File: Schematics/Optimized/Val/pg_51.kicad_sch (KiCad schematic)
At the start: 35 parts, among them U3501 F175, U3502 F175, U3503 F175, U5301 F158, U5302 F157, U5303 F02, U5304 F02, U5305 F74, U5306 F74, U5307 F02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

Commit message: TYP+VAL condensation
Tested: passed expmon_test_val (-muxbus)
Tested: passed expmon_test_typ (-muxbus)
Tested: passed run_udiag
Tested: passed boot_env (R2_INTEG until PRETTY_PRINTER)
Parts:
- removed U3501, U3502, U3503: F175, symbol r1000:F175
- removed U5301, U5401: F158, symbol r1000:F158
- removed U5302, U5310, U5311, U5312, U5406, U5408, U5410, U5411: F157, symbol r1000:F157
- removed U5303, U5304: F02, symbol r1000:F02
- removed U5313: F381, symbol r1000:F381
- removed U5407, U5421, U5422: F283, symbol r1000:F283
- removed U5409: F00, symbol r1000:F00
- removed U5420: F181, symbol r1000:F181
- added U2602: XCADR, symbol r1000:XCADR
- added U2609, U2616: F521, symbol r1000:F521
- added U2610, U2617: F74, symbol r1000:F74
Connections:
- net C.ALU.SEL0: now also U2602.74 (CTL0)
- net C.ALU.SEL1: now also U2602.75 (CTL1)
- net C.ALU.SEL2: now also U2602.76 (CTL2)
- net C.CSA.SEL: now also U2602.77 (CTL3)
- net C.LOOP.SEL: now also U2602.78 (CTL4)
- net C.ZERO.SEL: now also U2602.79 (CTL5)
- net CSA.DIAG0: now also U2602.21 (CSDG0)
- net CSA.DIAG1: now also U2602.23 (CSDG1)
- net CSA.DIAG2: now also U2602.25 (CSDG2)
- net CSA~.SCLK: now also U2602.4 (CCLK)
- net DIAG.D0: now also U2602.13 (DIAG0)
- net DIAG.D1: now also U2602.15 (DIAG1)
- net DIAG.D2: now also U2602.17 (DIAG2)
- net DIAG.D3: now also U2602.18 (DIAG3)
- net DIAG_MODE: now also U2602.10 (DMODE)
- net LOOP_CNT0: now also U2602.64 (LOOP0)
- net LOOP_CNT1: now also U2602.65 (LOOP1)
- net LOOP_CNT2: now also U2602.66 (LOOP2)
- net LOOP_CNT3: now also U2602.67 (LOOP3)
- net LOOP_CNT4: now also U2602.68 (LOOP4)
- net LOOP_CNT5: now also U2602.69 (LOOP5)
- net LOOP_CNT6: now also U2602.70 (LOOP6)
- net LOOP_CNT7: now also U2602.71 (LOOP7)
- net LOOP_CNT8: now also U2602.72 (LOOP8)
- net LOOP_CNT9: now also U2602.73 (LOOP9)
- net PD: now also U2609.1 (E), U2609.12 (B4), U2609.14 (B5), U2609.7 (B2), U2616.1 (E), U2616.12 (B4), U2616.14 (B5), U2616.7 (B2)
- net UIR.A2: now also U2602.32 (A2)
- net UIR.A3: now also U2602.34 (A3)
- net UIR.A4: now also U2602.36 (A4)
- net UIR.A5: now also U2602.37 (A5)
- net UIR.B2: now also U2602.44 (B2)
- net UIR.B3: now also U2602.46 (B3)
- net UIR.B4: now also U2602.47 (B4)
- net UIR.B5: now also U2602.49 (B5)
- net UIR.C0: now also U2602.51 (C0)
- net UIR.C1: now also U2602.52 (C1)
- net UIR.C2: now also U2602.53 (C2)
- net UIR.C3: now also U2602.54 (C3)
- net UIR.C4: now also U2602.55 (C4)
- net UIR.C5: now also U2602.56 (C5)
- net UIR.FRAME0: now also U2602.38 (FRM0)
- net UIR.FRAME1: now also U2602.39 (FRM1)
- net UIR.FRAME2: now also U2602.41 (FRM2)
- net UIR.FRAME3: now also U2602.43 (FRM3)
- net UIR.FRAME4: now also U2602.45 (FRM4)
- net UIR~.SCLK: now also U2602.1 (UCLK), U2610.3 (CLK), U2617.3 (CLK)
- net V.CSA.OFFS0: now also U2602.60 (CSAO0)
- net V.CSA.OFFS1: now also U2602.61 (CSAO1)
- net V.CSA.OFFS2: now also U2602.62 (CSAO2)
- net V.CSA.OFFS3: now also U2602.63 (CSAO3)
- net V.LOAD_BOT~: now also U2602.57 (LBOT)
- net V.LOAD_TOP~: now also U2602.58 (LTOP)
- net V.POP_DOWN~: now also U2602.59 (LPOP)
- new net: U2616.19 (A=B), U2617.2 (D)
- new net: U2609.19 (A=B), U2610.2 (D)
- new net ARF.ADR0: U2602.2 (AADR0)
- new net ARF.ADR1: U2602.3 (AADR1)
- new net ARF.ADR2: U2602.5 (AADR2)
- new net ARF.ADR3: U2602.6 (AADR3)
- new net ARF.ADR4: U2602.8 (AADR4)
- new net ARF.ADR5: U2602.9 (AADR5)
- new net ARF.ADR6: U2602.11 (AADR6)
- new net ARF.ADR7: U2602.12 (AADR7)
- new net ARF.ADR8: U2602.14 (AADR8)
- new net ARF.ADR9: U2602.16 (AADR9)
- new net A_LOOP_DEC: U2602.48 (ALOOP), U2617.6 (Q_)
- new net BRF.ADR0: U2602.19 (BADR0)
- new net BRF.ADR1: U2602.20 (BADR1)
- new net BRF.ADR2: U2602.22 (BADR2)
- new net BRF.ADR3: U2602.24 (BADR3)
- new net BRF.ADR4: U2602.26 (BADR4)
- new net BRF.ADR5: U2602.27 (BADR5)
- new net BRF.ADR6: U2602.29 (BADR6)
- new net BRF.ADR7: U2602.31 (BADR7)
- new net BRF.ADR8: U2602.33 (BADR8)
- new net BRF.ADR9: U2602.35 (BADR9)
- new net B_LOOP_DEC: U2602.50 (BLOOP), U2610.6 (Q_)
- new net H2: U2602.7 (H2)
- new net UIR.A0: U2602.28 (A0)
- new net UIR.A1: U2602.30 (A1)
- new net UIR.B0: U2602.40 (B0)
- new net UIR.B1: U2602.42 (B1)
- new net WCS.D0: U2616.6 (A2)
- new net WCS.D1: U2616.8 (A3)
- new net WCS.D10: U2609.15 (A6)
- new net WCS.D11: U2609.17 (A7)
- new net WCS.D2: U2616.11 (A4)
- new net WCS.D3: U2616.13 (A5)
- new net WCS.D4: U2616.15 (A6)
- new net WCS.D5: U2616.17 (A7)
- new net WCS.D6: U2609.6 (A2)
- new net WCS.D7: U2609.8 (A3)
- new net WCS.D8: U2609.11 (A4)
- new net WCS.D9: U2609.13 (A5)
- no-connect marks 44 -> 26
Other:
- note added: "UIR.A0"
- note added: "UIR.A1"
- note added: "UIR.A2"
- note added: "UIR.A3"
- note added: "UIR.A4"
- note added: "UIR.A5"
- note added: "UIR.B0"
- note added: "UIR.B1"
- note added: "UIR.B2"
- note added: "UIR.B3"
- note added: "UIR.B4"
- note added: "UIR.B5"
- moved on the sheet: GB11, GB13, GB17, GB3, GB4, GB5, GB6, GB7, GB8, U5305, U5306, U5307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

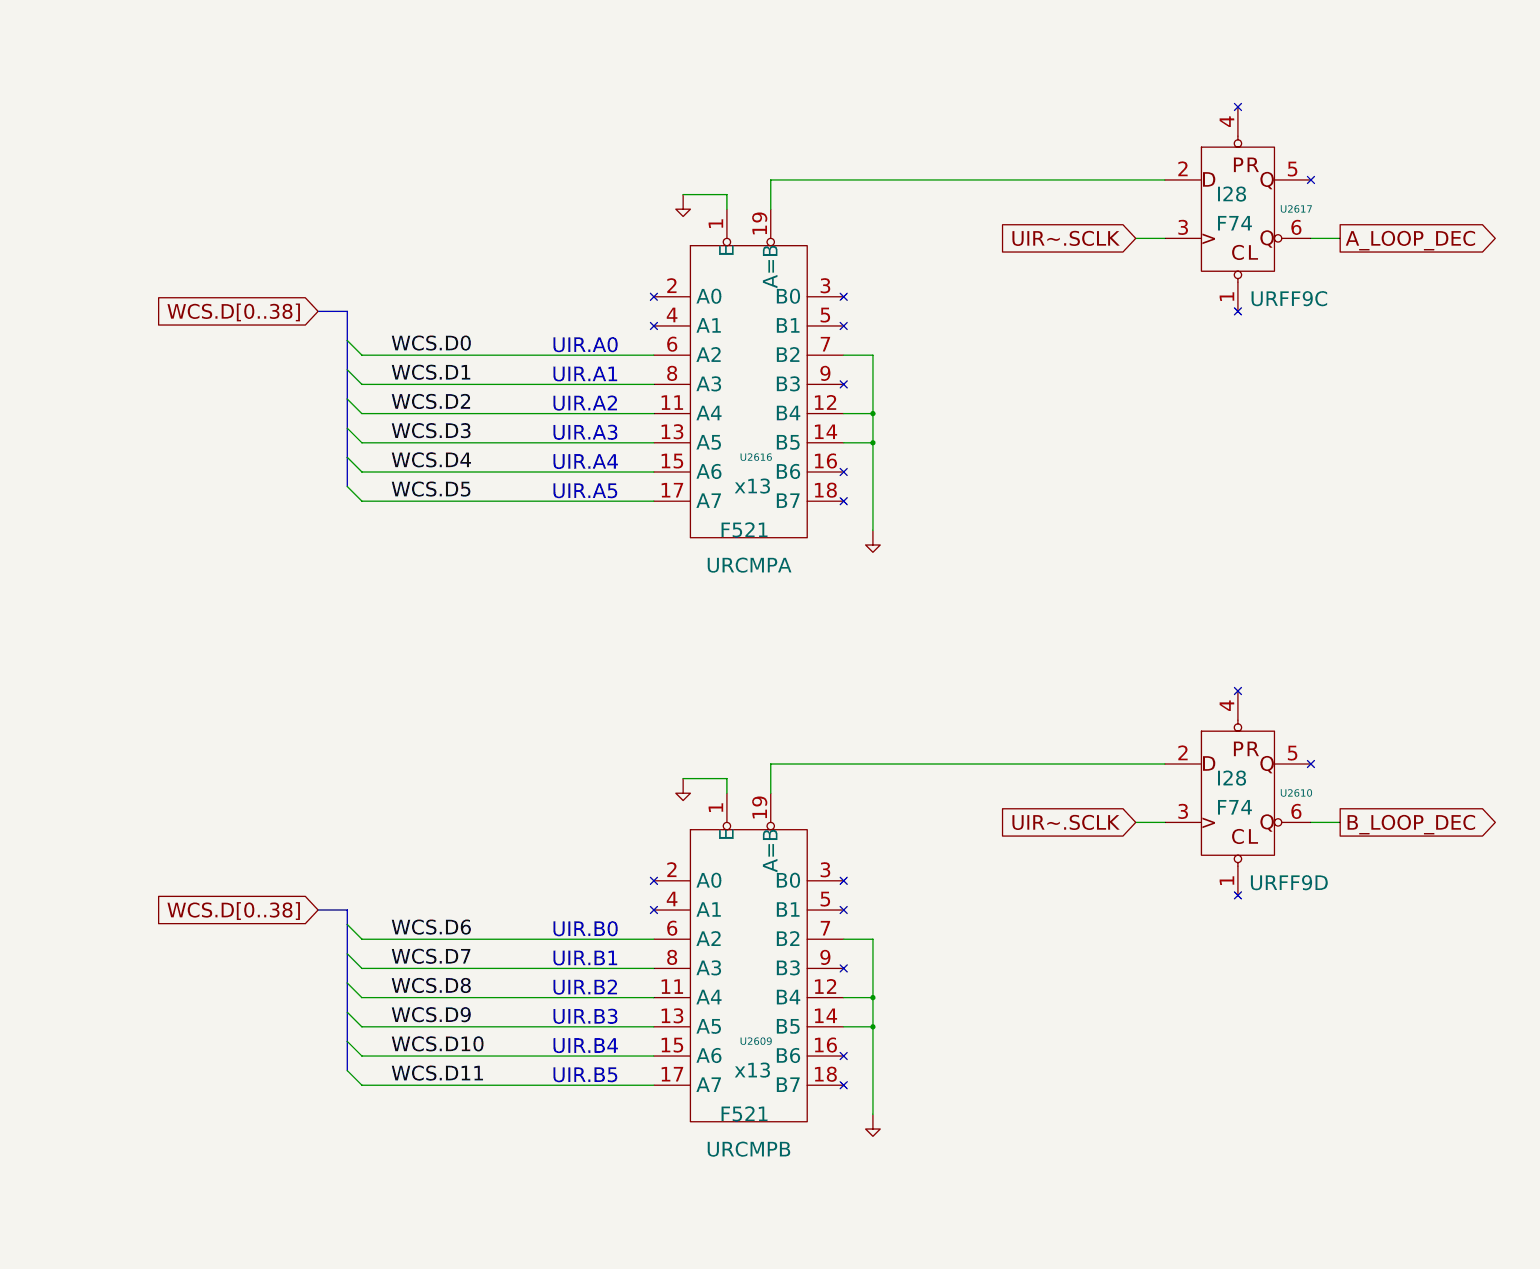
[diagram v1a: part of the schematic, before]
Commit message: Optimization of TYP & VAL
Tested: boot_env (until PRETTY_PRINTER assert)
Tested: passed run_udiag
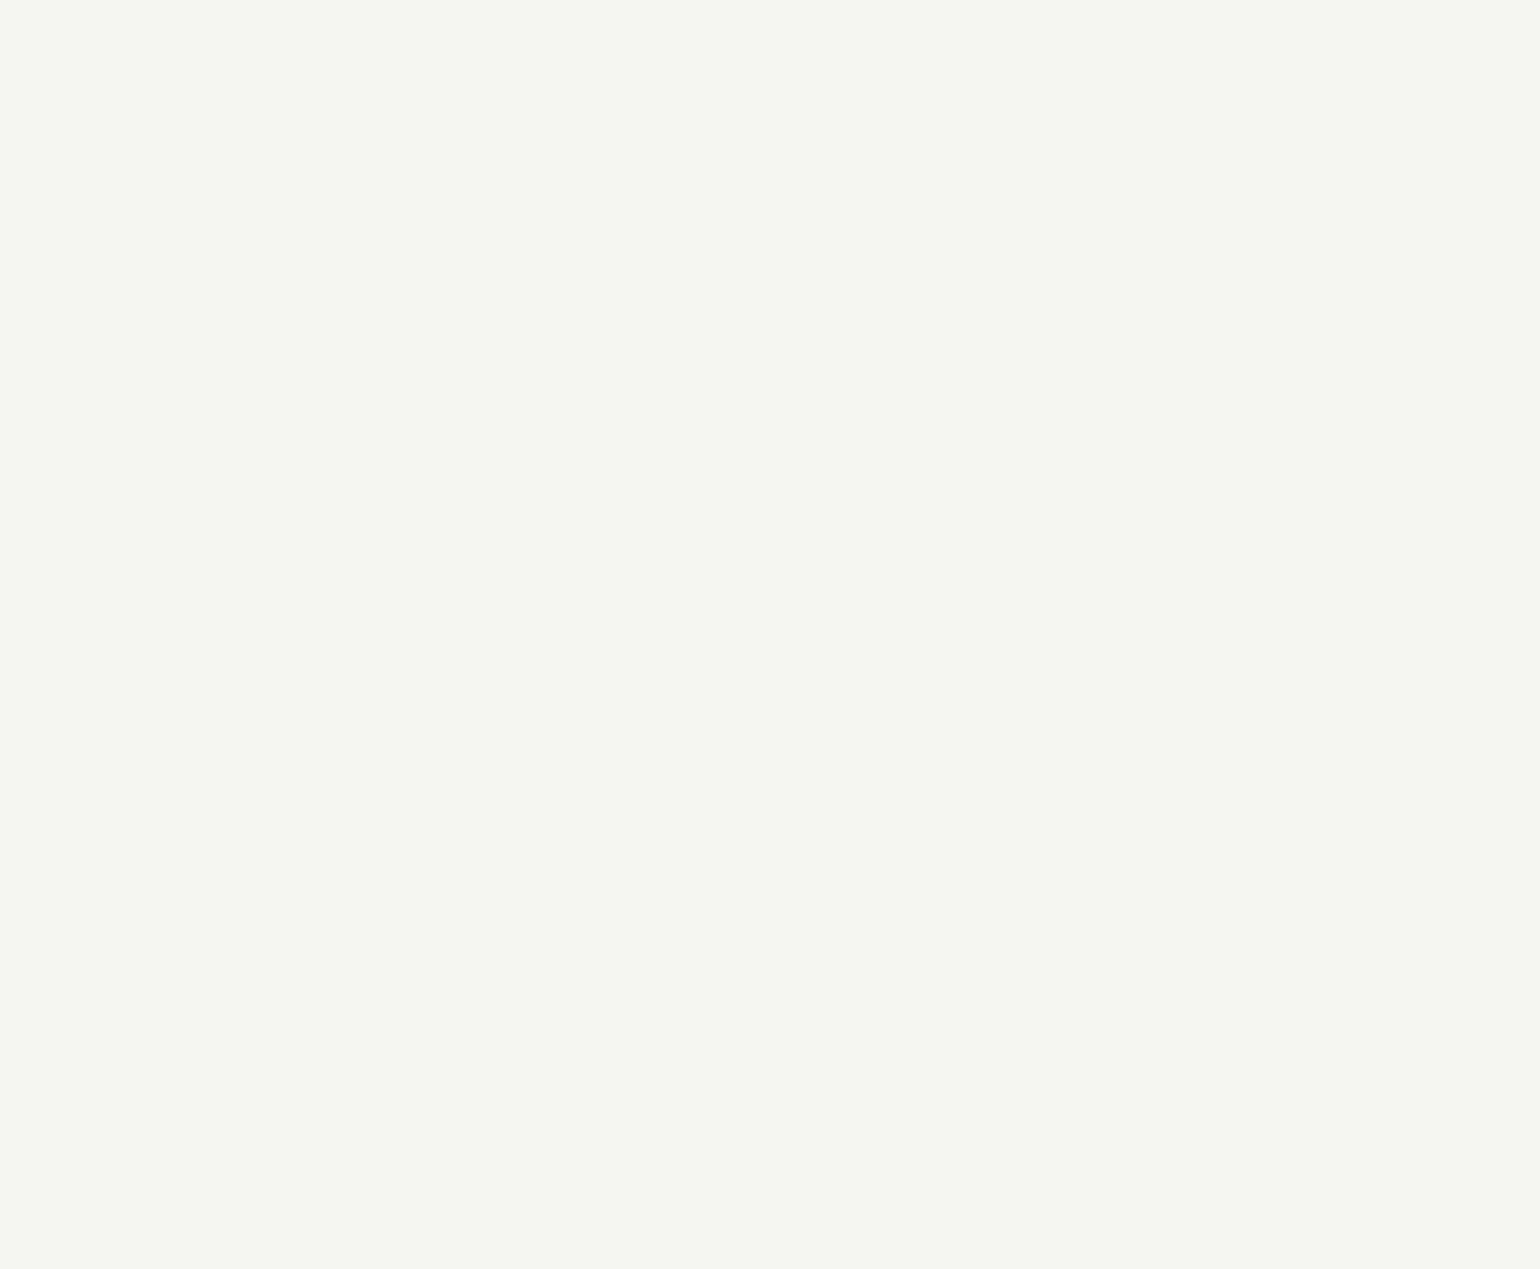
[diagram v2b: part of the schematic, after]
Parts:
- removed U2609, U2616: F521, symbol r1000:F521
- removed U2610, U2617: F74, symbol r1000:F74
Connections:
- no-connect marks 26 -> 6
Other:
- note removed: "UIR.A0"
- note removed: "UIR.A1"
- note removed: "UIR.A2"
- note removed: "UIR.A3"
- note removed: "UIR.A4"
- note removed: "UIR.A5"
- note removed: "UIR.B0"
- note removed: "UIR.B1"
- note removed: "UIR.B2"
- note removed: "UIR.B3"
- note removed: "UIR.B4"
- note removed: "UIR.B5"

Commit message: XCLKSTP, XIOP XSUDEC
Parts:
- removed U5308: F02, symbol r1000:F02
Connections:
- net CSA_WRITE_EN: now reaches U5307.3 (Q), U5309.19 (A0)
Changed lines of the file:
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@@
+    (stroke (width 0) (type default))
+  )
+  (wire (pts (xy 370.84 284.48) (xy 370.84 317.5))
     (stroke (width 0) (type default))
   )
@@
     (stroke (width 0) (type default))
   )
-  (wire (pts (xy 375.92 297.18) (xy 370.84 297.18))
-    (stroke (width 0) (type default))
-  )
   (wire (pts (xy 86.36 287.02) (xy 116.84 287.02))
     (stroke (width 0) (type default))
@@
     (stroke (width 0) (type default))
   )
+  (wire (pts (xy 370.84 284.48) (xy 375.92 284.48))
+    (stroke (width 0) (type default))
+  )
   (bus (pts (xy 195.58 68.58) (xy 190.5 68.58))
     (stroke (width 0) (type default))
@@
     (stroke (width 0) (type default))
   )
-  (wire (pts (xy 370.84 297.18) (xy 370.84 317.5))
-    (stroke (width 0) (type default))
-  )
   (wire (pts (xy 248.92 340.36) (xy 246.38 340.36))
     (stroke (width 0) (type default))
@@
     (stroke (width 0) (type default))
   )
-  (wire (pts (xy 398.78 294.64) (xy 406.4 294.64))
-    (stroke (width 0) (type default))
-  )
   (wire (pts (xy 88.9 256.54) (xy 116.84 256.54))
     (stroke (width 0) (type default))
@@
   )
   (bus (pts (xy 190.5 55.88) (xy 190.5 60.96))
-    (stroke (width 0) (type default))
-  )
-  (wire (pts (xy 370.84 292.1) (xy 375.92 292.1))
     (stroke (width 0) (type default))
   )
@@
     )
   )
-  (global_label "Q3~" (shape input) (at 370.84 292.1 180) (fields_autoplaced)
-    (effects (font (size 2.54 2.54)) (justify right))
-    (property "Intersheetrefs" "${INTERSHEET_REFS}" (at 358.1352 292.1 0)
-      (effects (font (size 1.905 1.905)) (justify right))
-    )
-  )
   (global_label "UIR.C5" (shape input) (at 111.76 200.66 180) (fields_autoplaced)
     (effects (font (size 2.54 2.54)) (justify right))
@@
     )
   )
+  (global_label "CSA_WRITE_EN" (shape output) (at 375.92 284.48 0) (fields_autoplaced)
+    (effects (font (size 2.54 2.54)) (justify left))
+    (property "Intersheetrefs" "${INTERSHEET_REFS}" (at 408.5818 284.48 0)
+      (effects (font (size 1.27 1.27)) (justify left))
+    )
+  )
   (global_label "UIR.B3" (shape input) (at 111.76 154.94 180) (fields_autoplaced)
     (effects (font (size 2.54 2.54)) (justify right))
@@
     (property "Intersheetrefs" "${INTERSHEET_REFS}" (at 193.0447 139.7 0)
       (effects (font (size 1.27 1.27)) (justify left))
-    )
-  )
-  (global_label "CSA_WRITE.EN~" (shape output) (at 406.4 294.64 0) (fields_autoplaced)
-    (effects (font (size 2.54 2.54)) (justify left))
-    (property "Intersheetrefs" "${INTERSHEET_REFS}" (at 439.166 294.4813 0)
-      (effects (font (size 1.905 1.905)) (justify left))
     )
   )
@@
         )
       )
-    )
-  )
-  (symbol (lib_id "r1000:F02") (at 383.54 292.1 0) (unit 1)
-    (in_bom yes) (on_board yes) (dnp no)
-    (property "Reference" "U5308" (at 395.7 291.465 0)
-      (effects (font (size 1.27 1.27)))
-    )
-    (property "Value" "F02" (at 382.27 296.545 0)
-      (effects (font (size 2.54 2.54)) (justify left))
-    )
-    (property "Footprint" "" (at 383.54 292.1 0)
-      (effects (font (size 1.27 1.27)) hide)
-    )
-    (property "Datasheet" "" (at 383.54 292.1 0)
-      (effects (font (size 1.27 1.27)) hide)
-    )
-    (property "Location" "M38" (at 386.08 292.1 0)
-      (effects (font (size 2.54 2.54)))
-    )
-    (property "Name" "RCNOR0D" (at 386.08 304.8 0)
-      (effects (font (size 2.54 2.54)) (justify bottom))
-    )
-    (pin "1")
-    (pin "2")
-    (pin "3")
-    (instances
-      (project "VAL"
-        (path "/20011966-0b12-5e7d-4f5d-7b7451992361/20011966-50f0-40db-7afe-07e89482cc87"
-          (reference "U5308") (unit 1)
-        )
-      )
